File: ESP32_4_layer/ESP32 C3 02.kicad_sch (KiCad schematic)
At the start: 30 parts, among them J3 GSD090012SEU_SDcard_Connector, U2 ESP32-C3-WROOM-02-H4, U3 CP2102N-Axx-xQFN20, U4 USBLC6-2SC6, U5 W25Q32JVSS

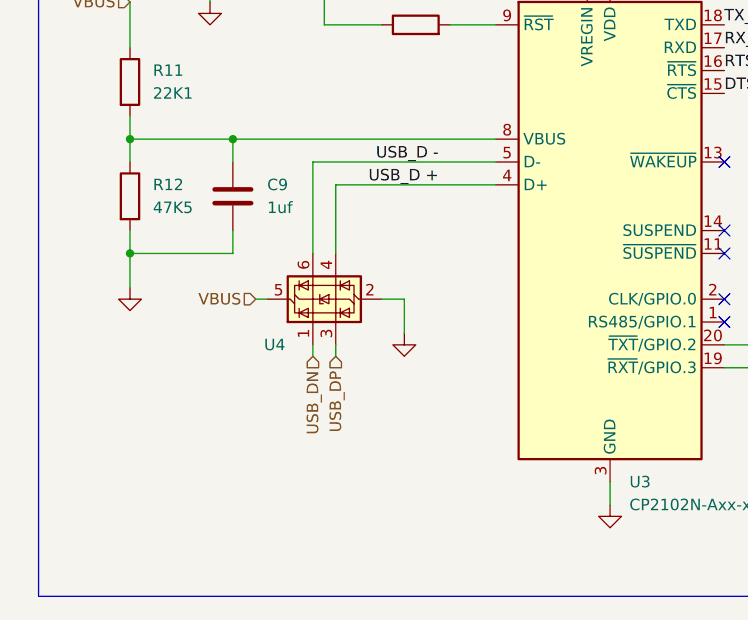
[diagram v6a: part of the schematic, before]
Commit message: upto inner layer copper zone
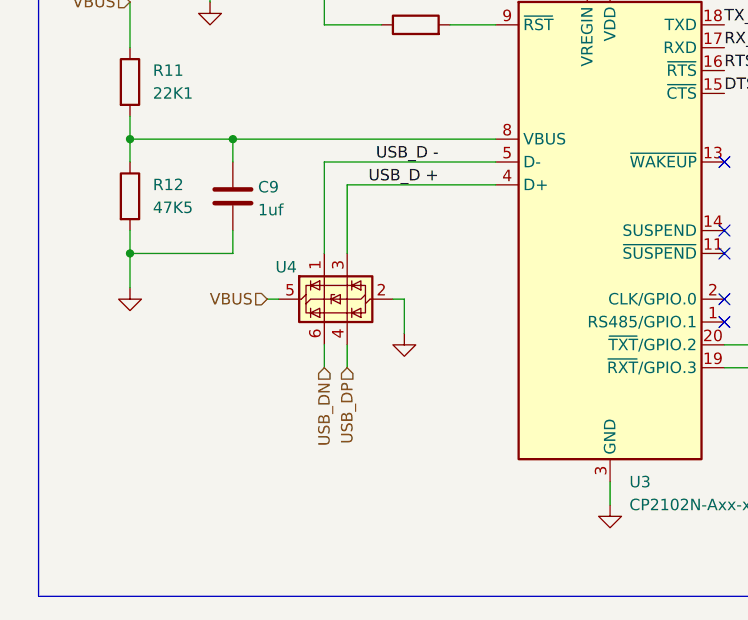
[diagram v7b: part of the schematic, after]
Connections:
- net USB_D +: now also U4.3 (I/O2); no longer U4.4 (I/O2)
- net USB_D -: now also U4.1 (I/O1); no longer U4.6 (I/O1)
- net USB_DN: now also U4.6 (I/O1); no longer U4.1 (I/O1)
- net USB_DP: now also U4.4 (I/O2); no longer U4.3 (I/O2)
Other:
- moved on the sheet: U4
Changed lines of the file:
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@@
-	(wire
-		(pts
-			(xy 55.88 83.82) (xy 55.88 82.55)
-		)
-		(stroke
-			(width 0)
-			(type default)
-		)
-	)
 	(wire
 		(pts
@@
 	(wire
 		(pts
+			(xy 48.26 77.47) (xy 49.53 77.47)
+		)
+		(stroke
+			(width 0)
+			(type default)
+		)
+	)
+	(wire
+		(pts
 			(xy 104.14 85.09) (xy 104.14 88.9)
 		)
@@
 	(wire
 		(pts
+			(xy 54.61 62.23) (xy 54.61 72.39)
+		)
+		(stroke
+			(width 0)
+			(type default)
+		)
+	)
+	(wire
+		(pts
 			(xy 227.33 40.64) (xy 229.87 40.64)
 		)
@@
 	(wire
 		(pts
-			(xy 55.88 64.77) (xy 73.66 64.77)
-		)
-		(stroke
-			(width 0)
-			(type default)
-		)
-	)
-	(wire
-		(pts
-			(xy 53.34 83.82) (xy 53.34 82.55)
-		)
-		(stroke
-			(width 0)
-			(type default)
-		)
-	)
-	(wire
-		(pts
 			(xy 251.46 153.67) (xy 254 153.67)
 		)
@@
 	(wire
 		(pts
-			(xy 53.34 62.23) (xy 53.34 72.39)
-		)
-		(stroke
-			(width 0)
-			(type default)
-		)
-	)
-	(wire
-		(pts
 			(xy 210.82 40.64) (xy 210.82 31.75)
 		)
@@
 	(wire
 		(pts
-			(xy 63.5 77.47) (xy 60.96 77.47)
+			(xy 57.15 85.09) (xy 57.15 82.55)
 		)
 		(stroke
@@
 	(wire
 		(pts
+			(xy 54.61 85.09) (xy 54.61 82.55)
+		)
+		(stroke
+			(width 0)
+			(type default)
+		)
+	)
+	(wire
+		(pts
 			(xy 271.78 154.94) (xy 270.51 154.94)
 		)
@@
 	(wire
 		(pts
-			(xy 55.88 64.77) (xy 55.88 72.39)
-		)
-		(stroke
-			(width 0)
-			(type default)
-		)
-	)
-	(wire
-		(pts
 			(xy 262.89 130.81) (xy 260.35 130.81)
 		)
@@
 	(wire
 		(pts
+			(xy 62.23 77.47) (xy 63.5 77.47)
+		)
+		(stroke
+			(width 0)
+			(type default)
+		)
+	)
+	(wire
+		(pts
 			(xy 114.3 142.24) (xy 116.84 142.24)
 		)
@@
 	(wire
 		(pts
+			(xy 57.15 64.77) (xy 57.15 72.39)
+		)
+		(stroke
+			(width 0)
+			(type default)
+		)
+	)
+	(wire
+		(pts
 			(xy 166.37 144.78) (xy 166.37 132.08)
 		)
@@
 	(wire
 		(pts
+			(xy 57.15 64.77) (xy 73.66 64.77)
+		)
+		(stroke
+			(width 0)
+			(type default)
+		)
+	)
+	(wire
+		(pts
 			(xy 81.28 135.89) (xy 76.2 135.89)
 		)
@@
 	(wire
 		(pts
-			(xy 46.99 77.47) (xy 48.26 77.47)
-		)
-		(stroke
-			(width 0)
-			(type default)
-		)
-	)
-	(wire
-		(pts
 			(xy 205.74 127) (xy 205.74 125.73)
 		)
@@
 	(wire
 		(pts
-			(xy 73.66 62.23) (xy 53.34 62.23)
+			(xy 73.66 62.23) (xy 54.61 62.23)
 		)
 		(stroke
@@
 			)
 			(justify left bottom)
-		)
-	)
-	(hierarchical_label "USB_DN"
-		(shape input)
-		(at 53.34 83.82 270)
-		(effects
-			(font
-				(size 1.27 1.27)
-			)
-			(justify right)
 		)
 	)
@@
 	(hierarchical_label "USB_DP"
 		(shape input)
-		(at 55.88 83.82 270)
+		(at 57.15 85.09 270)
+		(effects
+			(font
+				(size 1.27 1.27)
+			)
+			(justify right)
+		)
+	)
+	(hierarchical_label "USB_DN"
+		(shape input)
+		(at 54.61 85.09 270)
 		(effects
 			(font
@@
 	(hierarchical_label "VBUS"
 		(shape input)
-		(at 46.99 77.47 180)
+		(at 48.26 77.47 180)
 		(effects
 			(font
@@
 	(symbol
 		(lib_id "Power_Protection:USBLC6-2SC6")
-		(at 53.34 77.47 90)
+		(at 54.61 77.47 90)
+		(mirror x)
 		(unit 1)
 		(exclude_from_sim no)
@@
 		(dnp no)
 		(property "Reference" "U4"
-			(at 50.292 82.55 90)
+			(at 51.562 73.914 90)
 			(effects
 				(font
@@
 		)
 		(property "Value" "USBLC6-2SC6"
-			(at 48.26 75.8189 0)
+			(at 49.53 79.1211 0)
 			(effects
 				(font
@@
 		)
 		(property "Footprint" "Package_TO_SOT_SMD:SOT-23-6"
-			(at 59.69 76.2 0)
+			(at 60.96 78.74 0)
 			(effects
 				(font
@@
 		)
 		(property "Datasheet" "https://www.st.com/resource/en/datasheet/usblc6-2.pdf"
-			(at 61.595 76.2 0)
+			(at 62.865 78.74 0)
 			(effects
 				(font
@@
 		)
 		(property "Description" "Very low capacitance ESD protection diode, 2 data-line, SOT-23-6"
-			(at 53.34 77.47 0)
+			(at 54.61 77.47 0)
 			(effects
 				(font
@@
 		(on_board yes)
 		(dnp no)
-		(fields_autoplaced yes)
 		(property "Reference" "C9"
-			(at 48.26 64.7699 0)
+			(at 47.244 65.024 0)
 			(effects
 				(font
@@
 		)
 		(property "Value" "1uf"
-			(at 48.26 67.3099 0)
-			(effects
-				(font
+			(at 47.244 67.564 0)
+			(effects
+				(font
